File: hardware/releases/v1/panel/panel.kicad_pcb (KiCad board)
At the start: 4 copper layers, 146.5 x 52 mm, 121 parts, among them J1 12-32V + RS485, J2 Crown board, J201 Probe T-Header SMD, J3 Probe board, J301 CROWN_RISER, J4 PMSA003I PM, J401 Main board, J402 Reflector T-Socket SMD, J5 Power board, J501 Main board, Q1 AO3400A, Q401 AO3400A, SW1 SERVICE, U2 LM66100, U3 XIAO ESP32C6, U301 LTR-390UV-01, U302 TSL25911FN, U303 GUVB-C31SM, U4 ADS1115IDGSR, U401 SCD41-D-R2, U402 SGP41-D-R4, U403 SHT40-AD1F-R2, U404 LM2903DR2G, U405 BMP585, U5 LSM6DS3TR-C, U501 TPS54360DDAR, U502 TPS54360DDAR, U7 SP3485EN-L/TR

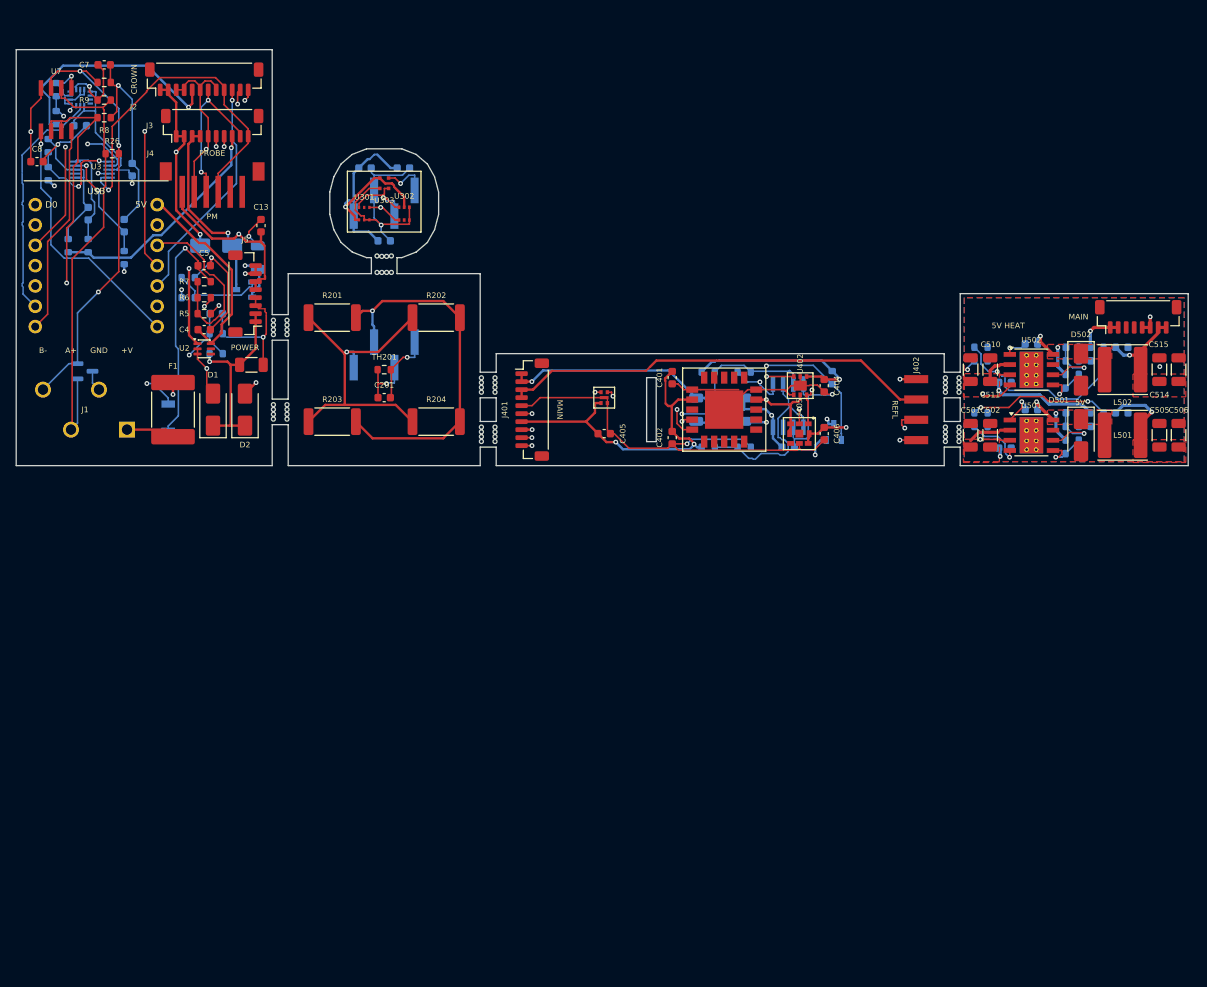
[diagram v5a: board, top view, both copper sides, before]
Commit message: Update documentation for column-packed breakaway panel, probe LDO rail, mast clamp dimensions, transducer adapter redesign, crown SWD/auto-flash workflow, and enclosure print plate organization
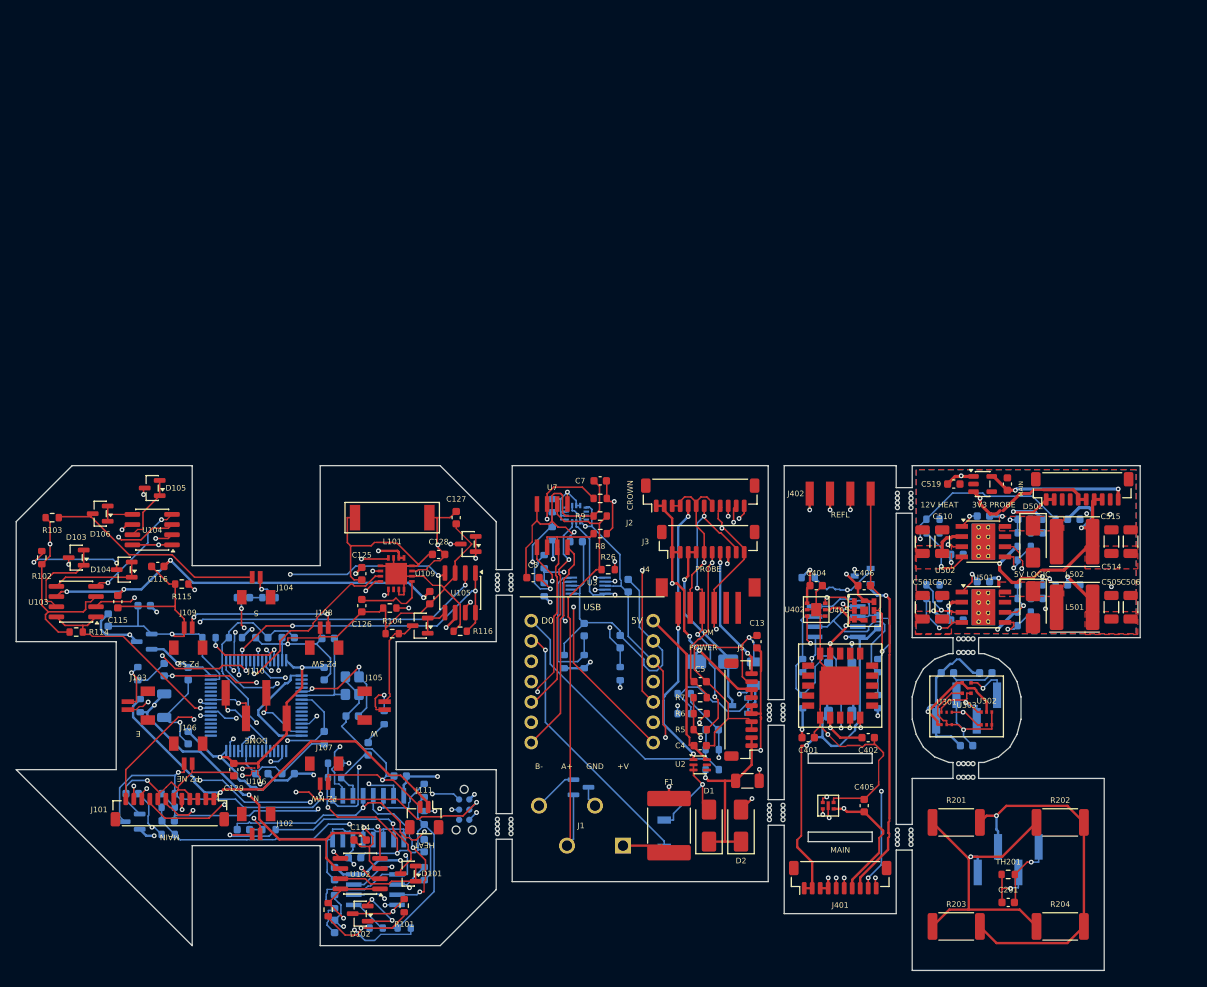
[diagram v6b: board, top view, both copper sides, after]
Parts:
- added C101: 1u 50V, Capacitor_SMD:C_0603_1608Metric, B.Cu at (11.5, 19.3)
- added C102: 10u 10V, Capacitor_SMD:C_0603_1608Metric, B.Cu at (16.0, 17.5)
- added C103: 100n 50V, Capacitor_SMD:C_0603_1608Metric, B.Cu at (38.5, 26.0)
- added C104: 100n 50V, Capacitor_SMD:C_0603_1608Metric, B.Cu at (21.5, 26.0)
- added C105: 100n 50V, Capacitor_SMD:C_0603_1608Metric, B.Cu at (21.5, 34.0)
- added C106: 100n 50V, Capacitor_SMD:C_0603_1608Metric, B.Cu at (34.0, 38.5)
- added C107: 10u 10V, Capacitor_SMD:C_0603_1608Metric, B.Cu at (30.7, 38.5)
- added C108: 1u 50V, Capacitor_SMD:C_0603_1608Metric, B.Cu at (34.0, 21.5)
- added C109: 100n 50V, Capacitor_SMD:C_0603_1608Metric, B.Cu at (30.7, 21.5)
- added C110: 100n 50V, Capacitor_SMD:C_0603_1608Metric, B.Cu at (38.5, 34.0)
- added C111: 33p C0G 50V, Capacitor_SMD:C_0603_1608Metric, B.Cu at (42.0, 31.3)
- added C112: 33p C0G 50V, Capacitor_SMD:C_0603_1608Metric, B.Cu at (39.0, 21.6)
- added C113: 22u 25V, Capacitor_SMD:C_1206_3216Metric, B.Cu at (18.5, 30.0)
- added C114: 1u 50V, Capacitor_SMD:C_0603_1608Metric, F.Cu at (43.0, 46.8)
- added C115: 1u 50V, Capacitor_SMD:C_0603_1608Metric, F.Cu at (12.7, 17.0)
- added C116: 1u 50V, Capacitor_SMD:C_0603_1608Metric, F.Cu at (17.7, 12.6)
- added C117: 1u 50V, Capacitor_SMD:C_0603_1608Metric, F.Cu at (51.7, 16.5)
- added C118: 1u 50V, Capacitor_SMD:C_0603_1608Metric, B.Cu at (42.3, 49.0)
- added C119: 100n 50V, Capacitor_SMD:C_0603_1608Metric, B.Cu at (51.0, 47.5)
- added C120: 220p C0G 50V, Capacitor_SMD:C_0603_1608Metric, B.Cu at (39.8, 57.6)
- added C121: 22n 50V, Capacitor_SMD:C_0603_1608Metric, B.Cu at (19.0, 44.4)
- added C122: 1n 50V, Capacitor_SMD:C_0603_1608Metric, B.Cu at (14.5, 41.0)
- added C123: 100n 50V, Capacitor_SMD:C_0603_1608Metric, B.Cu at (39.8, 51.0)
- added C124: 100n 50V, Capacitor_SMD:C_0603_1608Metric, B.Cu at (48.0, 38.8)
- added C125: 100n 50V, Capacitor_SMD:C_0603_1608Metric, F.Cu at (43.2, 13.5)
- added C126: 1u 50V, Capacitor_SMD:C_0603_1608Metric, F.Cu at (43.2, 17.5)
- added C127: 470p C0G 50V, Capacitor_SMD:C_0603_1608Metric, F.Cu at (55.0, 6.50)
- added C128: 470p C0G 50V, Capacitor_SMD:C_0603_1608Metric, F.Cu at (52.8, 11.1)
- added C129: 100n 50V, Capacitor_SMD:C_0603_1608Metric, F.Cu at (27.2, 38.0)
- added C130: 10n 50V, Capacitor_SMD:C_0603_1608Metric, B.Cu at (28.4, 45.5)
- added C131: 10n 50V, Capacitor_SMD:C_0603_1608Metric, B.Cu at (18.5, 25.5)
- added C132: 10n 50V, Capacitor_SMD:C_0603_1608Metric, B.Cu at (28.4, 16.5)
- added C133: 10n 50V, Capacitor_SMD:C_0603_1608Metric, B.Cu at (44.0, 35.4)
- added C519: 1u 50V, Capacitor_SMD:C_0603_1608Metric, F.Cu at (117.2, 2.30)
- added C520: 10u 10V, Capacitor_SMD:C_0603_1608Metric, F.Cu at (123.9, 2.30)
- added D101: BAV99, Package_TO_SOT_SMD:SOT-23, F.Cu at (49.0, 51.0)
- added D102: BAV99, Package_TO_SOT_SMD:SOT-23, F.Cu at (43.0, 56.0)
- added D103: BAV99, Package_TO_SOT_SMD:SOT-23, F.Cu at (7.50, 11.5)
- added D104: BAV99, Package_TO_SOT_SMD:SOT-23, F.Cu at (13.5, 13.0)
- added D105: BAV99, Package_TO_SOT_SMD:SOT-23, F.Cu at (17.0, 2.80)
- added D106: BAV99, Package_TO_SOT_SMD:SOT-23, F.Cu at (10.5, 6.00)
- added D107: BAV99, Package_TO_SOT_SMD:SOT-23, F.Cu at (56.5, 9.80)
- added D108: BAV99, Package_TO_SOT_SMD:SOT-23, F.Cu at (50.5, 20.0)
- added D109: BAV99, Package_TO_SOT_SMD:SOT-23, B.Cu at (14.5, 44.5)
- added J101: Main board, Connector_JST:JST_SH_BM12B-SRSS-TB_1x12-1MP_P1.00mm_Vertical, F.Cu at (19.2, 43.0)
- added J102: XD_N, gateway_fp:JST_BM02B-SRSS-TB, F.Cu at (30.0, 44.8)
- added J103: XD_E, gateway_fp:JST_BM02B-SRSS-TB, F.Cu at (15.2, 30.0)
- added J104: XD_S, gateway_fp:JST_BM02B-SRSS-TB, F.Cu at (30.0, 15.2)
- added J105: XD_W, gateway_fp:JST_BM02B-SRSS-TB, F.Cu at (44.8, 30.0)
- added J106: PIEZO_NE, gateway_fp:JST_BM02B-SRSS-TB, F.Cu at (21.5, 36.0)
- added J107: PIEZO_NW, gateway_fp:JST_BM02B-SRSS-TB, F.Cu at (38.5, 38.5)
- added J108: PIEZO_SW, gateway_fp:JST_BM02B-SRSS-TB, F.Cu at (38.5, 21.5)
- added J109: PIEZO_SE, gateway_fp:JST_BM02B-SRSS-TB, F.Cu at (21.5, 21.5)
- added J110: DOME_SOCKET, gateway_fp:HX_PZ2.54-1x4P-SMD, F.Cu at (30.0, 30.0)
- added J111: AUX 12V_HEAT, Connector_JST:JST_SH_BM02B-SRSS-TB_1x02-1MP_P1.00mm_Vertical, F.Cu at (51.0, 44.0)
- added J112: SWD, Connector:Tag-Connect_TC2030-IDC-NL_2x03_P1.27mm_Vertical, B.Cu at (56.0, 43.0)
- added L101: 100uH, RF_Antenna:Coilcraft_MA5532-AE_RFID, F.Cu at (47.0, 6.50)
- added R101: 330R, Resistor_SMD:R_0603_1608Metric, F.Cu at (48.5, 55.0)
- added R102: 330R, Resistor_SMD:R_0603_1608Metric, F.Cu at (3.20, 11.5)
- added R103: 330R, Resistor_SMD:R_0603_1608Metric, F.Cu at (4.50, 6.50)
- added R104: 330R, Resistor_SMD:R_0603_1608Metric, F.Cu at (47.0, 21.0)
- added R105: 47k, Resistor_SMD:R_0603_1608Metric, B.Cu at (31.6, 45.5)
- added R106: 47k, Resistor_SMD:R_0603_1608Metric, B.Cu at (15.2, 26.0)
- added R107: 47k, Resistor_SMD:R_0603_1608Metric, B.Cu at (31.6, 16.5)
- added R108: 47k, Resistor_SMD:R_0603_1608Metric, B.Cu at (46.0, 31.5)
- added R109: 1M, Resistor_SMD:R_0603_1608Metric, B.Cu at (51.0, 44.0)
- added R110: 1M, Resistor_SMD:R_0603_1608Metric, B.Cu at (51.0, 40.6)
- added R111: 1M, Resistor_SMD:R_0603_1608Metric, B.Cu at (39.8, 37.2)
- added R112: 1M, Resistor_SMD:R_0603_1608Metric, B.Cu at (39.8, 39.0)
- added R113: 4k7, Resistor_SMD:R_0603_1608Metric, F.Cu at (39.0, 55.5)
- added R114: 4k7, Resistor_SMD:R_0603_1608Metric, F.Cu at (7.50, 20.8)
- added R115: 4k7, Resistor_SMD:R_0603_1608Metric, F.Cu at (20.7, 14.8)
- added R116: 4k7, Resistor_SMD:R_0603_1608Metric, F.Cu at (55.5, 20.7)
- added R117: 10R, Resistor_SMD:R_0603_1608Metric, B.Cu at (15.5, 30.0)
- added R118: 10k, Resistor_SMD:R_0603_1608Metric, B.Cu at (48.5, 57.8)
- added R119: 10k, Resistor_SMD:R_0603_1608Metric, B.Cu at (45.0, 57.8)
- added R120: 1k, Resistor_SMD:R_0603_1608Metric, B.Cu at (51.0, 51.0)
- added R121: 6k8, Resistor_SMD:R_0603_1608Metric, B.Cu at (39.8, 54.5)
- added R122: 1k, Resistor_SMD:R_0603_1608Metric, B.Cu at (19.0, 41.0)
- added R123: 4M7, Resistor_SMD:R_0603_1608Metric, B.Cu at (19.0, 42.7)
- added R124: 1k, Resistor_SMD:R_0603_1608Metric, B.Cu at (19.0, 46.1)
- added R125: 10k, Resistor_SMD:R_0603_1608Metric, B.Cu at (24.1, 21.5)
- added R126: 10k, Resistor_SMD:R_0603_1608Metric, F.Cu at (46.7, 17.8)
- added R127: 10R, Resistor_SMD:R_0603_1608Metric, B.Cu at (27.4, 21.5)
- added U101: STM32G431RBT6, Package_QFP:LQFP-64_10x10mm_P0.5mm, B.Cu at (30.0, 30.0)
- added U102: UCC27524ADR, Package_SO:SOIC-8_3.9x4.9mm_P1.27mm, F.Cu at (43.0, 51.0)
- added U103: UCC27524ADR, Package_SO:SOIC-8_3.9x4.9mm_P1.27mm, F.Cu at (7.50, 17.0)
- added U104: UCC27524ADR, Package_SO:SOIC-8_3.9x4.9mm_P1.27mm, F.Cu at (17.0, 8.00)
- added U105: UCC27524ADR, Package_SO:SOIC-8_3.9x4.9mm_P1.27mm, F.Cu at (55.5, 15.9)
- added U106: MMC5603NJ, gateway_fp:MEMSIC_MMC5603NJ_WLCSP-4, F.Cu at (30.0, 38.0)
- added U107: 74HC4052D, gateway_fp:TI_CD4052BM96_SOIC-16, B.Cu at (44.0, 44.0)
- added U108: TLV9062IDR, gateway_fp:TI_TLV9062IDR_SOIC-8, B.Cu at (44.9, 53.0)
- added U109: AS3935-BQFT, gateway_fp:ScioSense_AS3935_QFN-16, F.Cu at (47.5, 13.5)
- added U110: XC6206P332MR, Package_TO_SOT_SMD:SOT-23, B.Cu at (16.0, 22.0)
- added U503: AP2112K-3.3, Package_TO_SOT_SMD:SOT-23-5, F.Cu at (120.8, 2.30)
- added Y101: 8MHz, Crystal:Crystal_SMD_3225-4Pin_3.2x2.5mm, B.Cu at (42.0, 27.5)
- J5, J501: footprint Connector_JST:JST_SH_BM08B-SRSS-TB_1x08-1MP_P1.00mm_Vertical -> Connector_JST:JST_SH_BM10B-SRSS-TB_1x10-1MP_P1.00mm_Vertical
- moved C201 100.3 mm to (124.0, 54.6)
- moved J201 100.3 mm to (124.0, 49.2)
- moved R201 100.3 mm to (117.5, 44.6)
- moved R202 100.3 mm to (130.5, 44.6)
- moved R203 100.3 mm to (117.5, 57.6)
- moved R204 100.3 mm to (130.5, 57.6)
- moved TH201 100.3 mm to (124.0, 51.1)
- moved C301 96.3 mm to (116.4, 25.9)
- moved C302 96.3 mm to (121.2, 25.9)
- moved C303 96.3 mm to (118.8, 35.0)
- moved U301 96.3 mm to (116.3, 31.6)
- moved U302 96.3 mm to (121.3, 31.6)
- moved J301 96.3 mm to (118.8, 30.3)
- moved U303 96.3 mm to (118.8, 27.8)
- moved C19 80.9 mm to (75.5, 22.0)
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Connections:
- net PROBE_+3V3 renamed PROBE_+3V3_PROBE
- J3 pad 7: +3V3 -> +3V3_PROBE
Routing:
- net CROWN_GND: track 0.00 -> 307.6 mm, vias 0 -> 15
- net CROWN_+3V3: track 0.00 -> 197.9 mm, vias 0 -> 12
- net CROWN_VDRV: track 0.00 -> 130.1 mm, vias 0 -> 8
- net CROWN_TX_P: track 0.00 -> 112.9 mm, vias 0 -> 8
- net CROWN_TX_N: track 0.00 -> 100.9 mm, vias 0 -> 6
- net CROWN_PIEZO_IN: track 0.00 -> 78.3 mm, vias 0 -> 4
- net CROWN_CROWN_NRST: track 0.00 -> 74.5 mm, vias 0 -> 4
- net CROWN_+3V3A: track 0.00 -> 70.5 mm, vias 0 -> 3
- net CROWN_US_VREF: track 0.00 -> 56.0 mm, vias 0 -> 2
- net CROWN_US_AMP_OUT: track 0.00 -> 52.5 mm, vias 0 -> 2
- net CROWN_+12V_HEAT: track 0.00 -> 52.2 mm, vias 0 -> 1
- net CROWN_SWCLK: track 0.00 -> 48.5 mm, vias 0 -> 2
- net CROWN_XD_EN_N: track 0.00 -> 48.3 mm, vias 0 -> 2
- net CROWN_XD_E_RX: track 0.00 -> 45.1 mm, vias 0 -> 3
- net CROWN_XD_N_B: track 0.00 -> 42.5 mm, vias 0 -> 2
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- added copper zone on In1.Cu, net CROWN_GND
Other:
- board size 146.5 x 52 mm -> 140.5 x 63.1 mm
- board text added: "12V HEAT"
- board text added: "3V3 PROBE"
- board text added: "5V LOGIC"
- board text added: "DOME"
- board text added: "E"
- board text added: "HEAT"
- board text added: "N"
- board text added: "PZ NE"
- board text added: "PZ NW"
- board text added: "PZ SE"
- board text added: "PZ SW"
- board text added: "S"
- board text added: "SWD"
- board text added: "W"
- board text removed: "5V"
- board text removed: "5V HEAT"

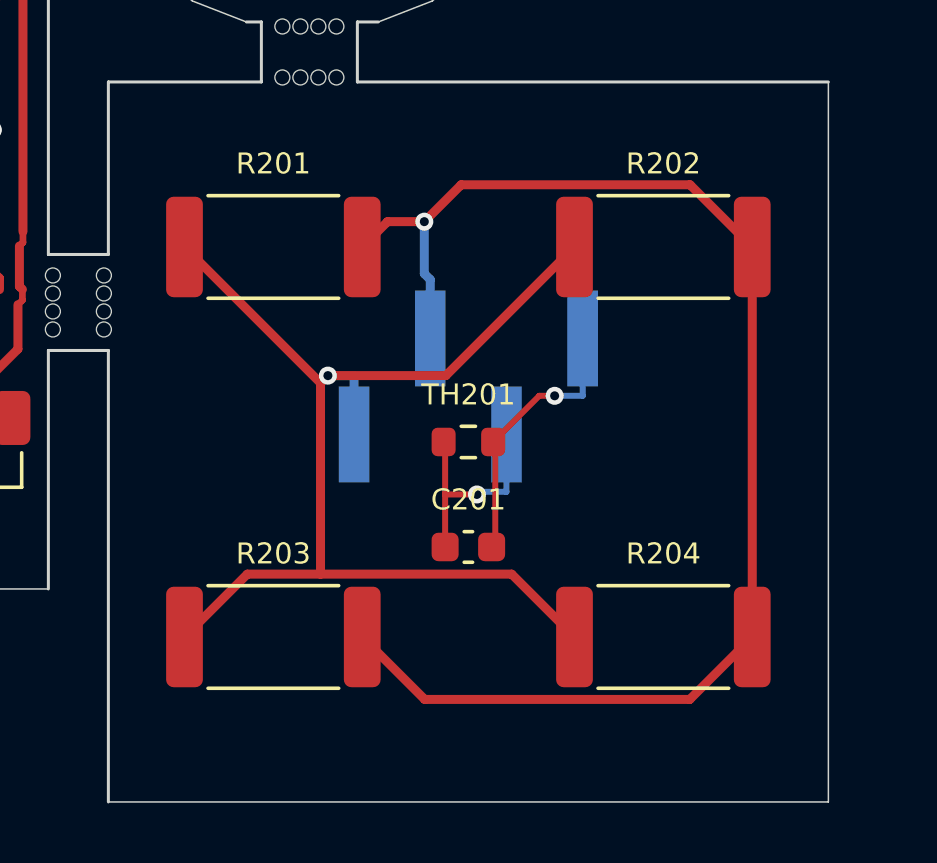
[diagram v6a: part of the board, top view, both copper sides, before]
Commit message: Update enclosure dimensions to 236 mm height, replace JGS1 hemisphere with stock Ø 20×2 mm window, add optional crown_dome variant for horizon view, update all PCB thickness to 1.6 mm, and revise UV sensor positioning
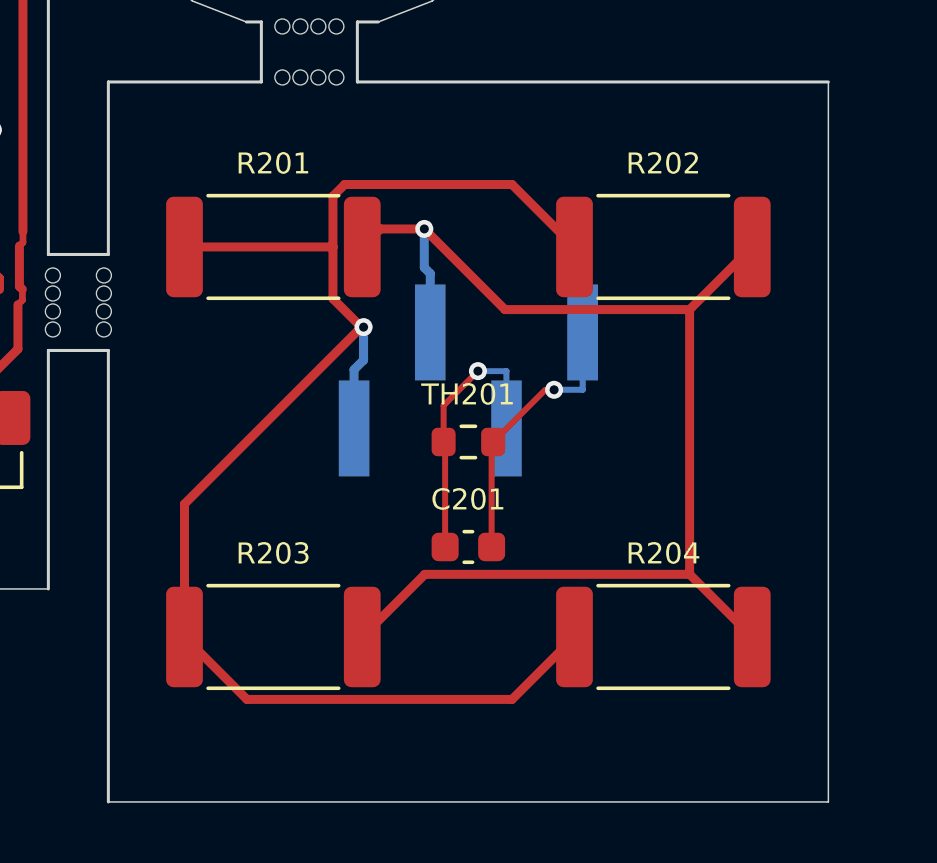
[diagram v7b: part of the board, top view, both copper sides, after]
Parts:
- moved J201 0.20 mm to (124.0, 49.0)
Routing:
- net REFLECTOR_+12V_HEAT: track 40.7 -> 49.9 mm
- net REFLECTOR_HEAT_SW: track 46.4 -> 42.3 mm
- net REFLECTOR_NTC_SENSE: track 7.51 -> 9.22 mm

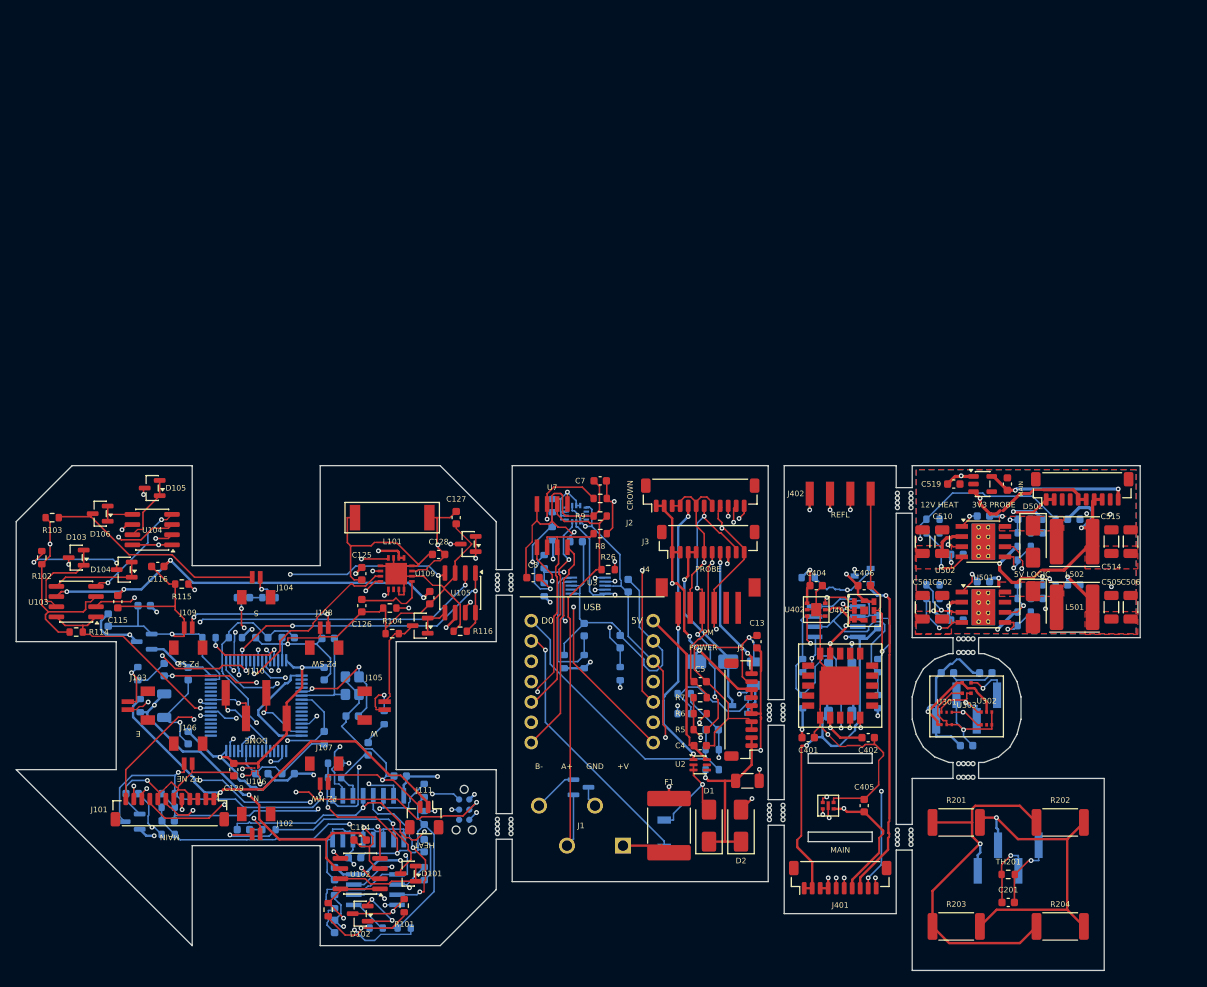
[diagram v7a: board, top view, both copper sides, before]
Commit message: Update AGENTS.md, CALIBRATION.md, and README.md for PTFE dome diffuser, probe heater setpoint change to −7.6 °C, crown preamp bias mode, RS-485 fail-safe bias note, and enclosure seal test
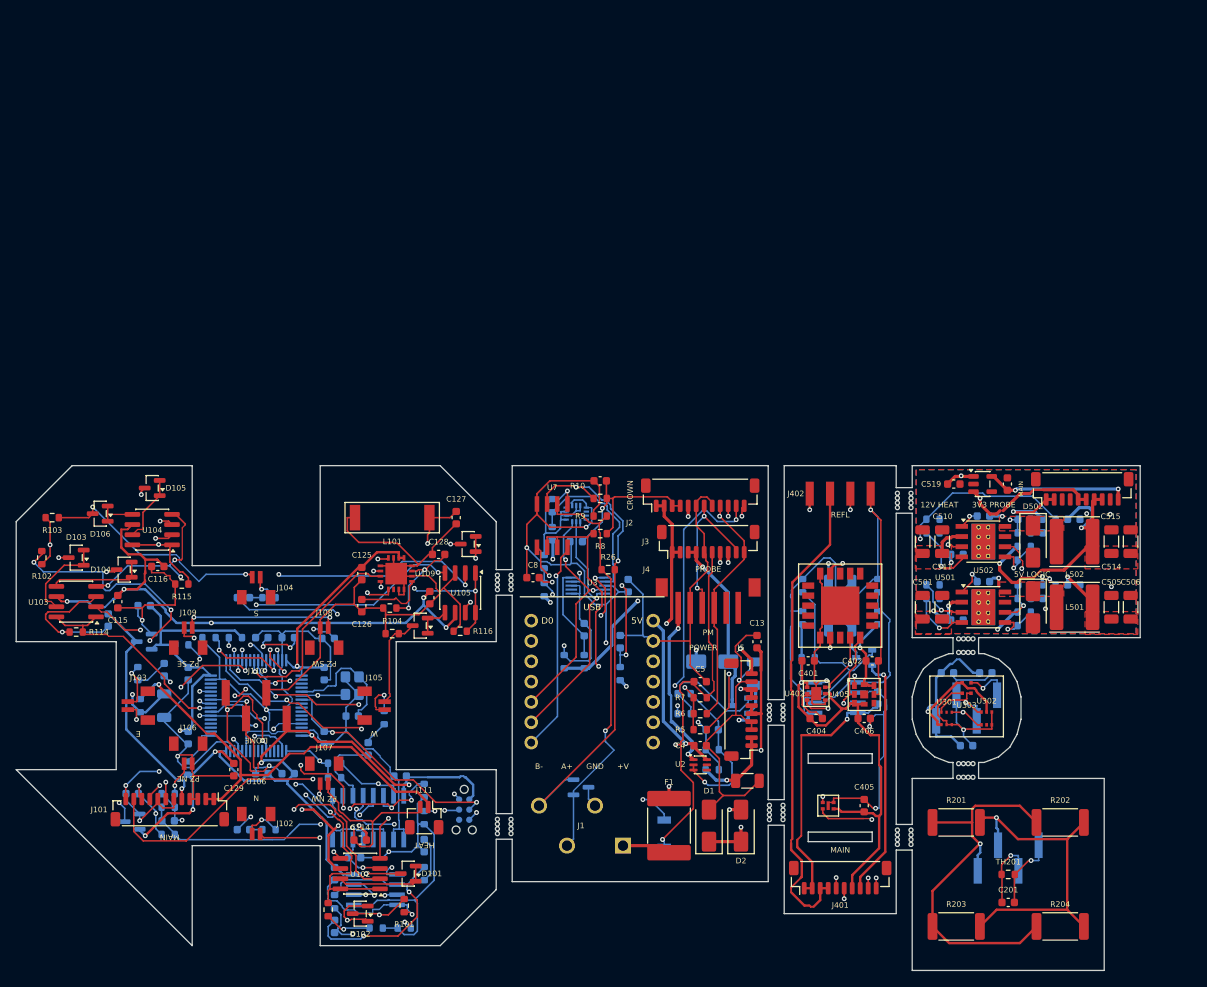
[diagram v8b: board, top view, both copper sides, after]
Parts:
- added R128: 10k, Resistor_SMD:R_0603_1608Metric, B.Cu at (20.7, 22.4)
- added R129: 10k, Resistor_SMD:R_0603_1608Metric, B.Cu at (21.4, 37.8)
- C125: value 100n 50V -> 1u 50V
- R124: value 1k -> 22k
- R405: value 22k -> 51k
- moved C404 16.6 mm to (100.0, 31.6)
- moved C406 16.6 mm to (106.0, 31.6)
- moved R401 10.5 mm to (103.0, 20.5)
- moved R402 10.5 mm to (103.0, 14.5)
- moved R403 10.5 mm to (98.3, 19.0)
- moved R404 10.5 mm to (107.7, 19.0)
- moved TH401 10.5 mm to (103.0, 17.5)
- moved U402 10.5 mm to (100.0, 28.5)
- moved U405 10.5 mm to (106.0, 28.6)
- moved Q401 10.2 mm to (106.0, 24.0)
- moved R405 10.0 mm to (107.7, 15.0)
- moved R406 10.0 mm to (99.0, 24.0)
- moved R407 10.0 mm to (98.3, 15.0)
- moved U401 10.0 mm to (103.0, 17.5)
- moved C402 9.61 mm to (107.0, 24.4)
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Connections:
- U101 pad 17: (no net) -> CROWN_US_VREF
- U101 pad 33: (no net) -> CROWN_BL_PB12
- U101 pad 44: (no net) -> CROWN_BL_PA10
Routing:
- net PROBE_I2C_SDA: track 73.7 -> 48.2 mm, vias 6 -> 4
- net CROWN_+3V3: track 197.9 -> 176.0 mm, vias 12 -> 8
- net CROWN_XD_E_RX: track 45.1 -> 64.9 mm, vias 3 -> 4
- net CROWN_GND: track 307.6 -> 325.9 mm, vias 15 -> 14
- net GND: track 150.8 -> 169.1 mm, vias 8 -> 7
- net CROWN_US_VREF: track 56.0 -> 72.2 mm
- net CROWN_XD_N_B: track 42.5 -> 28.3 mm
- net CROWN_US_AMP_FB: track 20.4 -> 32.8 mm
- net CROWN_VDRV: track 130.1 -> 142.4 mm, vias 8 -> 9
- net HEAT_PWM: track 21.1 -> 33.1 mm
- net PROBE_I2C_SCL: track 59.3 -> 47.5 mm
- net PROBE_CO2_HEAT_RTN: track 41.3 -> 30.4 mm
- net CROWN_CROWN_BOOT0: track 36.6 -> 46.2 mm, vias 3 -> 4
- net CROWN_TX_N: track 100.9 -> 110.3 mm, vias 6 -> 7
- net CROWN_XD_N_OUT_B: track 27.0 -> 17.6 mm, vias 3 -> 2
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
